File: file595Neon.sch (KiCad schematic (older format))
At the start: 33 parts, among them U1 74HC595

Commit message: First row
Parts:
- removed D1, D2, D3, D4, D5, D6, D7, D8: Q_TRIAC_A1GA2, Package_TO_SOT_SMD:SOT-23, symbol Device:Q_TRIAC_A1GA2
- removed NE1, NE2, NE3, NE4, NE5, NE6, NE7, NE8: Lamp_Neon, Connector_PinHeader_2.54mm:PinHeader_1x02_P2.54mm_Horizontal, symbol Device:Lamp_Neon
- removed R1, R11, R13, R15, R3, R5, R7, R9: 330k, Resistor_SMD:R_0402_1005Metric, symbol Device:R
- removed R10, R12, R14, R16, R2, R4, R6, R8: 33k, Resistor_SMD:R_0603_1608Metric, symbol Device:R
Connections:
- net sheet5EF2B64C/SIGNAL: now reaches U1.1 (QB)
- net SheetSingleBulb/SIGNAL: now reaches U1.15 (QA)
- net sheet5EF2B6E0/SIGNAL: now reaches U1.2 (QC)
- net sheet5EF2B77E/SIGNAL: now reaches U1.3 (QD)
- net sheet5EF2B800/SIGNAL: now reaches U1.4 (QE)
- net sheet5EF2B8A4/SIGNAL: now reaches U1.5 (QF)
- net sheet5EF2B938/SIGNAL: now reaches U1.6 (QG)
- net sheet5EF2B9F4/SIGNAL: now reaches U1.7 (QH)
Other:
- moved on the sheet: U1

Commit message: Add isolation
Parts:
- added C?: 100n, Capacitor_SMD:C_0805_2012Metric, symbol Device:C
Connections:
- net +3V3: now also C?.1
- net GND: now also C?.2
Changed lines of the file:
@@
 $Descr A4 11693 8268
 encoding utf-8
-Sheet 2 73
+Sheet 11 73
 Title ""
 Date ""
@@
 AR Path="/5EFAAFE1/5EF2DDAB" Ref="U7"  Part="1"
 AR Path="/5EFAAFEB/5EF2DDAB" Ref="U8"  Part="1"
-F 0 "U1" H 1850 3500 50  0000 C CNN
+F 0 "U2" H 1850 3500 50  0000 C CNN
 F 1 "74HC595" H 2300 3500 50  0000 C CNN
 F 2 "Package_SO:SOIC-16_3.9x9.9mm_P1.27mm" H 2100 2950 50  0001 C CNN
@@
 AR Path="/5EFAAFE1/5EF2DDB1" Ref="#PWR0227"  Part="1"
 AR Path="/5EFAAFEB/5EF2DDB1" Ref="#PWR0248"  Part="1"
-F 0 "#PWR0101" H 2100 2200 50  0001 C CNN
+F 0 "#PWR0122" H 2100 2200 50  0001 C CNN
 F 1 "+3V3" H 2115 2523 50  0000 C CNN
 F 2 "" H 2100 2350 50  0001 C CNN
@@
 AR Path="/5EFAAFE1/5EF2DDB7" Ref="#PWR0228"  Part="1"
 AR Path="/5EFAAFEB/5EF2DDB7" Ref="#PWR0249"  Part="1"
-F 0 "#PWR0102" H 2100 3400 50  0001 C CNN
+F 0 "#PWR0123" H 2100 3400 50  0001 C CNN
 F 1 "GND" H 2105 3477 50  0000 C CNN
 F 2 "" H 2100 3650 50  0001 C CNN
@@
 AR Path="/5EFAAFE1/5EF2DDC1" Ref="#PWR0229"  Part="1"
 AR Path="/5EFAAFEB/5EF2DDC1" Ref="#PWR0250"  Part="1"
-F 0 "#PWR0103" H 1350 2700 50  0001 C CNN
+F 0 "#PWR0124" H 1350 2700 50  0001 C CNN
 F 1 "+3V3" H 1365 3023 50  0000 C CNN
 F 2 "" H 1350 2850 50  0001 C CNN
@@
 AR Path="/5EFAAFE1/5EF2DDEA" Ref="#PWR0230"  Part="1"
 AR Path="/5EFAAFEB/5EF2DDEA" Ref="#PWR0251"  Part="1"
-F 0 "#PWR0104" H 1050 1100 50  0001 C CNN
+F 0 "#PWR0125" H 1050 1100 50  0001 C CNN
 F 1 "NEUT" H 1065 1423 50  0000 C CNN
 F 2 "" H 1050 1250 50  0001 C CNN
@@
 AR Path="/5EFAAFE1/5EF2DDF0" Ref="#PWR0231"  Part="1"
 AR Path="/5EFAAFEB/5EF2DDF0" Ref="#PWR0252"  Part="1"
-F 0 "#PWR0105" H 1200 1000 50  0001 C CNN
+F 0 "#PWR0126" H 1200 1000 50  0001 C CNN
 F 1 "GND" H 1205 1077 50  0000 C CNN
 F 2 "" H 1200 1250 50  0001 C CNN
@@
 Wire Wire Line
 	2500 2850 4350 2850
+$Comp
+L Device:C C?
+U 1 1 5EFA360C
+P 800 2900
+AR Path="/5EFA360C" Ref="C?"  Part="1"
+AR Path="/5EFA92A6/5EFA360C" Ref="C?"  Part="1"
+F 0 "C?" H 915 2946 50  0000 L CNN
+F 1 "100n" H 915 2855 50  0000 L CNN
+F 2 "Capacitor_SMD:C_0805_2012Metric" H 838 2750 50  0001 C CNN
+F 3 "~" H 800 2900 50  0001 C CNN
+F 4 "C49678" H 800 2900 50  0001 C CNN "LCSC"
+	1    800  2900
+	1    0    0    -1
+$EndComp
+$Comp
+L power:+3V3 #PWR?
+U 1 1 5EFA3A68
+P 800 2750
+F 0 "#PWR?" H 800 2600 50  0001 C CNN
+F 1 "+3V3" H 815 2923 50  0000 C CNN
+F 2 "" H 800 2750 50  0001 C CNN
+F 3 "" H 800 2750 50  0001 C CNN
+	1    800  2750
+	1    0    0    -1
+$EndComp
+$Comp
+L power:GND #PWR?
+U 1 1 5EFA3F80
+P 800 3050
+F 0 "#PWR?" H 800 2800 50  0001 C CNN
+F 1 "GND" H 805 2877 50  0000 C CNN
+F 2 "" H 800 3050 50  0001 C CNN
+F 3 "" H 800 3050 50  0001 C CNN
+	1    800  3050
+	1    0    0    -1
+$EndComp
 $EndSCHEMATC

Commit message: Add routing
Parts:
- gave numbers to parts that had none: 1
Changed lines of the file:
@@
 $Descr A4 11693 8268
 encoding utf-8
-Sheet 11 73
+Sheet 2 73
 Title ""
 Date ""
@@
 AR Path="/5EFAAFE1/5EF2DDAB" Ref="U7"  Part="1"
 AR Path="/5EFAAFEB/5EF2DDAB" Ref="U8"  Part="1"
-F 0 "U2" H 1850 3500 50  0000 C CNN
+F 0 "U1" H 1850 3500 50  0000 C CNN
 F 1 "74HC595" H 2300 3500 50  0000 C CNN
 F 2 "Package_SO:SOIC-16_3.9x9.9mm_P1.27mm" H 2100 2950 50  0001 C CNN
@@
 AR Path="/5EFAAFE1/5EF2DDB1" Ref="#PWR0227"  Part="1"
 AR Path="/5EFAAFEB/5EF2DDB1" Ref="#PWR0248"  Part="1"
-F 0 "#PWR0122" H 2100 2200 50  0001 C CNN
+F 0 "#PWR0101" H 2100 2200 50  0001 C CNN
 F 1 "+3V3" H 2115 2523 50  0000 C CNN
 F 2 "" H 2100 2350 50  0001 C CNN
@@
 AR Path="/5EFAAFE1/5EF2DDB7" Ref="#PWR0228"  Part="1"
 AR Path="/5EFAAFEB/5EF2DDB7" Ref="#PWR0249"  Part="1"
-F 0 "#PWR0123" H 2100 3400 50  0001 C CNN
+F 0 "#PWR0102" H 2100 3400 50  0001 C CNN
 F 1 "GND" H 2105 3477 50  0000 C CNN
 F 2 "" H 2100 3650 50  0001 C CNN
@@
 AR Path="/5EFAAFE1/5EF2DDC1" Ref="#PWR0229"  Part="1"
 AR Path="/5EFAAFEB/5EF2DDC1" Ref="#PWR0250"  Part="1"
-F 0 "#PWR0124" H 1350 2700 50  0001 C CNN
+F 0 "#PWR0103" H 1350 2700 50  0001 C CNN
 F 1 "+3V3" H 1365 3023 50  0000 C CNN
 F 2 "" H 1350 2850 50  0001 C CNN
@@
 AR Path="/5EFAAFE1/5EF2DDEA" Ref="#PWR0230"  Part="1"
 AR Path="/5EFAAFEB/5EF2DDEA" Ref="#PWR0251"  Part="1"
-F 0 "#PWR0125" H 1050 1100 50  0001 C CNN
+F 0 "#PWR0104" H 1050 1100 50  0001 C CNN
 F 1 "NEUT" H 1065 1423 50  0000 C CNN
 F 2 "" H 1050 1250 50  0001 C CNN
@@
 AR Path="/5EFAAFE1/5EF2DDF0" Ref="#PWR0231"  Part="1"
 AR Path="/5EFAAFEB/5EF2DDF0" Ref="#PWR0252"  Part="1"
-F 0 "#PWR0126" H 1200 1000 50  0001 C CNN
+F 0 "#PWR0105" H 1200 1000 50  0001 C CNN
 F 1 "GND" H 1205 1077 50  0000 C CNN
 F 2 "" H 1200 1250 50  0001 C CNN
@@
 P 800 2900
 AR Path="/5EFA360C" Ref="C?"  Part="1"
-AR Path="/5EFA92A6/5EFA360C" Ref="C?"  Part="1"
-F 0 "C?" H 915 2946 50  0000 L CNN
+AR Path="/5EFA92A6/5EFA360C" Ref="C7"  Part="1"
+AR Path="/5EF299B0/5EFA360C" Ref="C6"  Part="1"
+AR Path="/5EFA93EC/5EFA360C" Ref="C8"  Part="1"
+AR Path="/5EFA9520/5EFA360C" Ref="C9"  Part="1"
+AR Path="/5EFAAFCD/5EFA360C" Ref="C10"  Part="1"
+AR Path="/5EFAAFD7/5EFA360C" Ref="C11"  Part="1"
+AR Path="/5EFAAFE1/5EFA360C" Ref="C12"  Part="1"
+AR Path="/5EFAAFEB/5EFA360C" Ref="C13"  Part="1"
+F 0 "C6" H 915 2946 50  0000 L CNN
 F 1 "100n" H 915 2855 50  0000 L CNN
 F 2 "Capacitor_SMD:C_0805_2012Metric" H 838 2750 50  0001 C CNN
@@
 $EndComp
 $Comp
-L power:+3V3 #PWR?
+L power:+3V3 #PWR0279
 U 1 1 5EFA3A68
 P 800 2750
-F 0 "#PWR?" H 800 2600 50  0001 C CNN
+AR Path="/5EFA92A6/5EFA3A68" Ref="#PWR0279"  Part="1"
+AR Path="/5EF299B0/5EFA3A68" Ref="#PWR0277"  Part="1"
+AR Path="/5EFA93EC/5EFA3A68" Ref="#PWR0281"  Part="1"
+AR Path="/5EFA9520/5EFA3A68" Ref="#PWR0283"  Part="1"
+AR Path="/5EFAAFCD/5EFA3A68" Ref="#PWR0285"  Part="1"
+AR Path="/5EFAAFD7/5EFA3A68" Ref="#PWR0287"  Part="1"
+AR Path="/5EFAAFE1/5EFA3A68" Ref="#PWR0289"  Part="1"
+AR Path="/5EFAAFEB/5EFA3A68" Ref="#PWR0291"  Part="1"
+F 0 "#PWR0277" H 800 2600 50  0001 C CNN
 F 1 "+3V3" H 815 2923 50  0000 C CNN
 F 2 "" H 800 2750 50  0001 C CNN
@@
 $EndComp
 $Comp
-L power:GND #PWR?
+L power:GND #PWR0280
 U 1 1 5EFA3F80
 P 800 3050
-F 0 "#PWR?" H 800 2800 50  0001 C CNN
+AR Path="/5EFA92A6/5EFA3F80" Ref="#PWR0280"  Part="1"
+AR Path="/5EF299B0/5EFA3F80" Ref="#PWR0278"  Part="1"
+AR Path="/5EFA93EC/5EFA3F80" Ref="#PWR0282"  Part="1"
+AR Path="/5EFA9520/5EFA3F80" Ref="#PWR0284"  Part="1"
+AR Path="/5EFAAFCD/5EFA3F80" Ref="#PWR0286"  Part="1"
+AR Path="/5EFAAFD7/5EFA3F80" Ref="#PWR0288"  Part="1"
+AR Path="/5EFAAFE1/5EFA3F80" Ref="#PWR0290"  Part="1"
+AR Path="/5EFAAFEB/5EFA3F80" Ref="#PWR0292"  Part="1"
+F 0 "#PWR0278" H 800 2800 50  0001 C CNN
 F 1 "GND" H 805 2877 50  0000 C CNN
 F 2 "" H 800 3050 50  0001 C CNN

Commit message: Add PCB markings
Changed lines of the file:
@@
 $Descr A4 11693 8268
 encoding utf-8
-Sheet 2 73
+Sheet 29 73
 Title ""
 Date ""
@@
 AR Path="/5EFAAFE1/5EF2DDAB" Ref="U7"  Part="1"
 AR Path="/5EFAAFEB/5EF2DDAB" Ref="U8"  Part="1"
-F 0 "U1" H 1850 3500 50  0000 C CNN
+F 0 "U8" H 1850 3500 50  0000 C CNN
 F 1 "74HC595" H 2300 3500 50  0000 C CNN
 F 2 "Package_SO:SOIC-16_3.9x9.9mm_P1.27mm" H 2100 2950 50  0001 C CNN
@@
 AR Path="/5EFAAFE1/5EF2DDB1" Ref="#PWR0227"  Part="1"
 AR Path="/5EFAAFEB/5EF2DDB1" Ref="#PWR0248"  Part="1"
-F 0 "#PWR0101" H 2100 2200 50  0001 C CNN
+F 0 "#PWR0248" H 2100 2200 50  0001 C CNN
 F 1 "+3V3" H 2115 2523 50  0000 C CNN
 F 2 "" H 2100 2350 50  0001 C CNN
@@
 AR Path="/5EFAAFE1/5EF2DDB7" Ref="#PWR0228"  Part="1"
 AR Path="/5EFAAFEB/5EF2DDB7" Ref="#PWR0249"  Part="1"
-F 0 "#PWR0102" H 2100 3400 50  0001 C CNN
+F 0 "#PWR0249" H 2100 3400 50  0001 C CNN
 F 1 "GND" H 2105 3477 50  0000 C CNN
 F 2 "" H 2100 3650 50  0001 C CNN
@@
 AR Path="/5EFAAFE1/5EF2DDC1" Ref="#PWR0229"  Part="1"
 AR Path="/5EFAAFEB/5EF2DDC1" Ref="#PWR0250"  Part="1"
-F 0 "#PWR0103" H 1350 2700 50  0001 C CNN
+F 0 "#PWR0250" H 1350 2700 50  0001 C CNN
 F 1 "+3V3" H 1365 3023 50  0000 C CNN
 F 2 "" H 1350 2850 50  0001 C CNN
@@
 AR Path="/5EFAAFE1/5EF2DDEA" Ref="#PWR0230"  Part="1"
 AR Path="/5EFAAFEB/5EF2DDEA" Ref="#PWR0251"  Part="1"
-F 0 "#PWR0104" H 1050 1100 50  0001 C CNN
+F 0 "#PWR0251" H 1050 1100 50  0001 C CNN
 F 1 "NEUT" H 1065 1423 50  0000 C CNN
 F 2 "" H 1050 1250 50  0001 C CNN
@@
 AR Path="/5EFAAFE1/5EF2DDF0" Ref="#PWR0231"  Part="1"
 AR Path="/5EFAAFEB/5EF2DDF0" Ref="#PWR0252"  Part="1"
-F 0 "#PWR0105" H 1200 1000 50  0001 C CNN
+F 0 "#PWR0252" H 1200 1000 50  0001 C CNN
 F 1 "GND" H 1205 1077 50  0000 C CNN
 F 2 "" H 1200 1250 50  0001 C CNN
@@
 AR Path="/5EFAAFE1/5EFA360C" Ref="C12"  Part="1"
 AR Path="/5EFAAFEB/5EFA360C" Ref="C13"  Part="1"
-F 0 "C6" H 915 2946 50  0000 L CNN
+F 0 "C13" H 915 2946 50  0000 L CNN
 F 1 "100n" H 915 2855 50  0000 L CNN
 F 2 "Capacitor_SMD:C_0805_2012Metric" H 838 2750 50  0001 C CNN
@@
 AR Path="/5EFAAFE1/5EFA3A68" Ref="#PWR0289"  Part="1"
 AR Path="/5EFAAFEB/5EFA3A68" Ref="#PWR0291"  Part="1"
-F 0 "#PWR0277" H 800 2600 50  0001 C CNN
+F 0 "#PWR0291" H 800 2600 50  0001 C CNN
 F 1 "+3V3" H 815 2923 50  0000 C CNN
 F 2 "" H 800 2750 50  0001 C CNN
@@
 AR Path="/5EFAAFE1/5EFA3F80" Ref="#PWR0290"  Part="1"
 AR Path="/5EFAAFEB/5EFA3F80" Ref="#PWR0292"  Part="1"
-F 0 "#PWR0278" H 800 2800 50  0001 C CNN
+F 0 "#PWR0292" H 800 2800 50  0001 C CNN
 F 1 "GND" H 805 2877 50  0000 C CNN
 F 2 "" H 800 3050 50  0001 C CNN

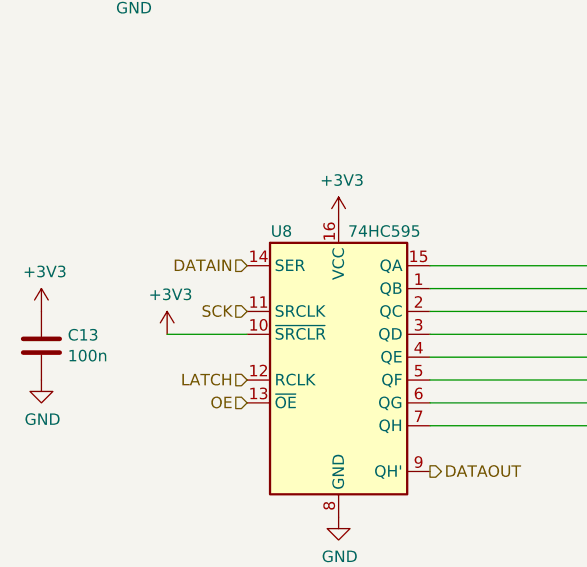
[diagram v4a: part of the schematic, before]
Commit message: Add bulk capacitance, fix isolation, silkscreen and vias
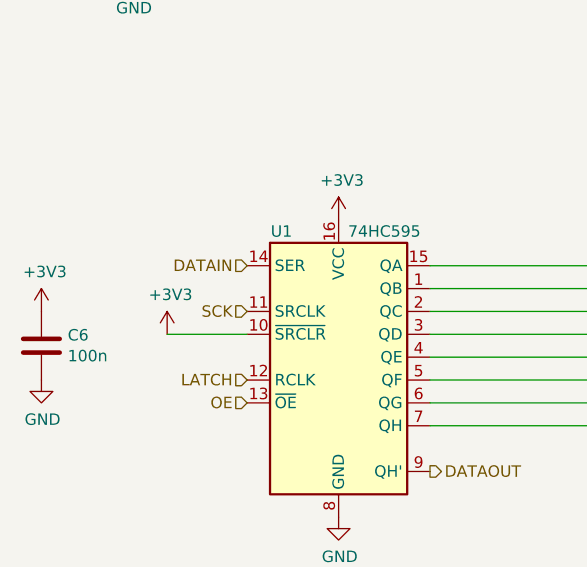
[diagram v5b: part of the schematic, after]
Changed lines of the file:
@@
 $Descr A4 11693 8268
 encoding utf-8
-Sheet 29 73
+Sheet 2 73
 Title ""
 Date ""
@@
 AR Path="/5EFAAFE1/5EF2DDAB" Ref="U7"  Part="1"
 AR Path="/5EFAAFEB/5EF2DDAB" Ref="U8"  Part="1"
-F 0 "U8" H 1850 3500 50  0000 C CNN
+F 0 "U1" H 1850 3500 50  0000 C CNN
 F 1 "74HC595" H 2300 3500 50  0000 C CNN
 F 2 "Package_SO:SOIC-16_3.9x9.9mm_P1.27mm" H 2100 2950 50  0001 C CNN
@@
 AR Path="/5EFAAFE1/5EF2DDB1" Ref="#PWR0227"  Part="1"
 AR Path="/5EFAAFEB/5EF2DDB1" Ref="#PWR0248"  Part="1"
-F 0 "#PWR0248" H 2100 2200 50  0001 C CNN
+F 0 "#PWR0101" H 2100 2200 50  0001 C CNN
 F 1 "+3V3" H 2115 2523 50  0000 C CNN
 F 2 "" H 2100 2350 50  0001 C CNN
@@
 AR Path="/5EFAAFE1/5EF2DDB7" Ref="#PWR0228"  Part="1"
 AR Path="/5EFAAFEB/5EF2DDB7" Ref="#PWR0249"  Part="1"
-F 0 "#PWR0249" H 2100 3400 50  0001 C CNN
+F 0 "#PWR0102" H 2100 3400 50  0001 C CNN
 F 1 "GND" H 2105 3477 50  0000 C CNN
 F 2 "" H 2100 3650 50  0001 C CNN
@@
 AR Path="/5EFAAFE1/5EF2DDC1" Ref="#PWR0229"  Part="1"
 AR Path="/5EFAAFEB/5EF2DDC1" Ref="#PWR0250"  Part="1"
-F 0 "#PWR0250" H 1350 2700 50  0001 C CNN
+F 0 "#PWR0103" H 1350 2700 50  0001 C CNN
 F 1 "+3V3" H 1365 3023 50  0000 C CNN
 F 2 "" H 1350 2850 50  0001 C CNN
@@
 AR Path="/5EFAAFE1/5EF2DDEA" Ref="#PWR0230"  Part="1"
 AR Path="/5EFAAFEB/5EF2DDEA" Ref="#PWR0251"  Part="1"
-F 0 "#PWR0251" H 1050 1100 50  0001 C CNN
+F 0 "#PWR0104" H 1050 1100 50  0001 C CNN
 F 1 "NEUT" H 1065 1423 50  0000 C CNN
 F 2 "" H 1050 1250 50  0001 C CNN
@@
 AR Path="/5EFAAFE1/5EF2DDF0" Ref="#PWR0231"  Part="1"
 AR Path="/5EFAAFEB/5EF2DDF0" Ref="#PWR0252"  Part="1"
-F 0 "#PWR0252" H 1200 1000 50  0001 C CNN
+F 0 "#PWR0105" H 1200 1000 50  0001 C CNN
 F 1 "GND" H 1205 1077 50  0000 C CNN
 F 2 "" H 1200 1250 50  0001 C CNN
@@
 AR Path="/5EFAAFE1/5EFA360C" Ref="C12"  Part="1"
 AR Path="/5EFAAFEB/5EFA360C" Ref="C13"  Part="1"
-F 0 "C13" H 915 2946 50  0000 L CNN
+F 0 "C6" H 915 2946 50  0000 L CNN
 F 1 "100n" H 915 2855 50  0000 L CNN
 F 2 "Capacitor_SMD:C_0805_2012Metric" H 838 2750 50  0001 C CNN
@@
 AR Path="/5EFAAFE1/5EFA3A68" Ref="#PWR0289"  Part="1"
 AR Path="/5EFAAFEB/5EFA3A68" Ref="#PWR0291"  Part="1"
-F 0 "#PWR0291" H 800 2600 50  0001 C CNN
+F 0 "#PWR0277" H 800 2600 50  0001 C CNN
 F 1 "+3V3" H 815 2923 50  0000 C CNN
 F 2 "" H 800 2750 50  0001 C CNN
@@
 AR Path="/5EFAAFE1/5EFA3F80" Ref="#PWR0290"  Part="1"
 AR Path="/5EFAAFEB/5EFA3F80" Ref="#PWR0292"  Part="1"
-F 0 "#PWR0292" H 800 2800 50  0001 C CNN
+F 0 "#PWR0278" H 800 2800 50  0001 C CNN
 F 1 "GND" H 805 2877 50  0000 C CNN
 F 2 "" H 800 3050 50  0001 C CNN

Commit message: RevA, Add production files
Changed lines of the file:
@@
 AR Path="/5EFAAFE1/5EF2DDAB" Ref="U7"  Part="1"
 AR Path="/5EFAAFEB/5EF2DDAB" Ref="U8"  Part="1"
-F 0 "U1" H 1850 3500 50  0000 C CNN
+F 0 "U8" H 1850 3500 50  0000 C CNN
 F 1 "74HC595" H 2300 3500 50  0000 C CNN
 F 2 "Package_SO:SOIC-16_3.9x9.9mm_P1.27mm" H 2100 2950 50  0001 C CNN
@@
 AR Path="/5EFAAFE1/5EF2DDB1" Ref="#PWR0227"  Part="1"
 AR Path="/5EFAAFEB/5EF2DDB1" Ref="#PWR0248"  Part="1"
-F 0 "#PWR0101" H 2100 2200 50  0001 C CNN
+F 0 "#PWR0248" H 2100 2200 50  0001 C CNN
 F 1 "+3V3" H 2115 2523 50  0000 C CNN
 F 2 "" H 2100 2350 50  0001 C CNN
@@
 AR Path="/5EFAAFE1/5EF2DDB7" Ref="#PWR0228"  Part="1"
 AR Path="/5EFAAFEB/5EF2DDB7" Ref="#PWR0249"  Part="1"
-F 0 "#PWR0102" H 2100 3400 50  0001 C CNN
+F 0 "#PWR0249" H 2100 3400 50  0001 C CNN
 F 1 "GND" H 2105 3477 50  0000 C CNN
 F 2 "" H 2100 3650 50  0001 C CNN
@@
 AR Path="/5EFAAFE1/5EF2DDC1" Ref="#PWR0229"  Part="1"
 AR Path="/5EFAAFEB/5EF2DDC1" Ref="#PWR0250"  Part="1"
-F 0 "#PWR0103" H 1350 2700 50  0001 C CNN
+F 0 "#PWR0250" H 1350 2700 50  0001 C CNN
 F 1 "+3V3" H 1365 3023 50  0000 C CNN
 F 2 "" H 1350 2850 50  0001 C CNN
@@
 AR Path="/5EFAAFE1/5EF2DDEA" Ref="#PWR0230"  Part="1"
 AR Path="/5EFAAFEB/5EF2DDEA" Ref="#PWR0251"  Part="1"
-F 0 "#PWR0104" H 1050 1100 50  0001 C CNN
+F 0 "#PWR0251" H 1050 1100 50  0001 C CNN
 F 1 "NEUT" H 1065 1423 50  0000 C CNN
 F 2 "" H 1050 1250 50  0001 C CNN
@@
 AR Path="/5EFAAFE1/5EF2DDF0" Ref="#PWR0231"  Part="1"
 AR Path="/5EFAAFEB/5EF2DDF0" Ref="#PWR0252"  Part="1"
-F 0 "#PWR0105" H 1200 1000 50  0001 C CNN
+F 0 "#PWR0252" H 1200 1000 50  0001 C CNN
 F 1 "GND" H 1205 1077 50  0000 C CNN
 F 2 "" H 1200 1250 50  0001 C CNN
@@
 AR Path="/5EFAAFE1/5EFA360C" Ref="C12"  Part="1"
 AR Path="/5EFAAFEB/5EFA360C" Ref="C13"  Part="1"
-F 0 "C6" H 915 2946 50  0000 L CNN
+F 0 "C13" H 915 2946 50  0000 L CNN
 F 1 "100n" H 915 2855 50  0000 L CNN
 F 2 "Capacitor_SMD:C_0805_2012Metric" H 838 2750 50  0001 C CNN
@@
 AR Path="/5EFAAFE1/5EFA3A68" Ref="#PWR0289"  Part="1"
 AR Path="/5EFAAFEB/5EFA3A68" Ref="#PWR0291"  Part="1"
-F 0 "#PWR0277" H 800 2600 50  0001 C CNN
+F 0 "#PWR0291" H 800 2600 50  0001 C CNN
 F 1 "+3V3" H 815 2923 50  0000 C CNN
 F 2 "" H 800 2750 50  0001 C CNN
@@
 AR Path="/5EFAAFE1/5EFA3F80" Ref="#PWR0290"  Part="1"
 AR Path="/5EFAAFEB/5EFA3F80" Ref="#PWR0292"  Part="1"
-F 0 "#PWR0278" H 800 2800 50  0001 C CNN
+F 0 "#PWR0292" H 800 2800 50  0001 C CNN
 F 1 "GND" H 805 2877 50  0000 C CNN
 F 2 "" H 800 3050 50  0001 C CNN
